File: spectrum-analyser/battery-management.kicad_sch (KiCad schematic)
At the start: 11 parts, among them J2 Conn_01x02, Q3 Q_NMOS_GSD, Q4 Q_NMOS_GSD, U5 AP9101CK6, U6 MCP73831-2-OT

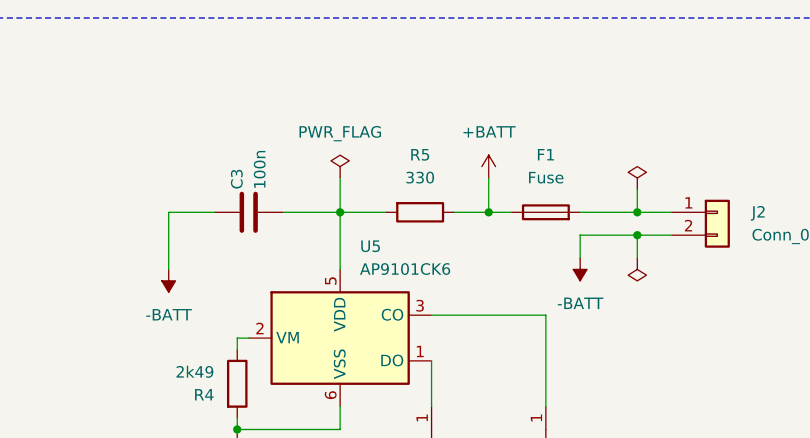
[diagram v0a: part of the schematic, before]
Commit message: Assign component footprints
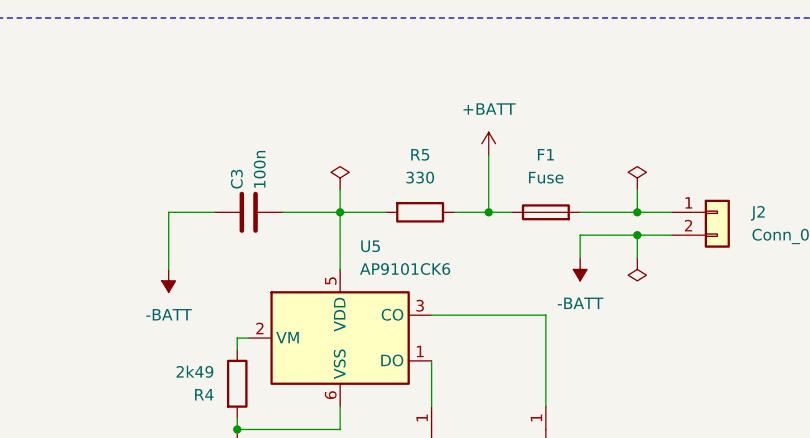
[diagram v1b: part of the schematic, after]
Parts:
- C3: footprint Capacitor_SMD:C_0603_1608Metric -> Capacitor_SMD:C_0603_1608Metric_Pad1.08x0.95mm_HandSolder
- F1: footprint (none) -> Fuse:Fuse_0603_1608Metric_Pad1.05x0.95mm_HandSolder
- J2: footprint (none) -> Connector_PinHeader_2.54mm:PinHeader_1x02_P2.54mm_Vertical
- JP1: footprint (none) -> Jumper:SolderJumper-2_P1.3mm_Open_RoundedPad1.0x1.5mm
- R4, R5: footprint Resistor_SMD:R_0603_1608Metric -> Resistor_SMD:R_0603_1608Metric_Pad0.98x0.95mm_HandSolder
- R6: footprint (none) -> Resistor_SMD:R_0603_1608Metric_Pad0.98x0.95mm_HandSolder
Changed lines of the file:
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@@
+	(wire
+		(pts
+			(xy 118.11 69.85) (xy 118.11 76.2)
+		)
+		(stroke
+			(width 0)
+			(type default)
+		)
+	)
 	(wire
 		(pts
@@
 	(wire
 		(pts
-			(xy 101.6 72.39) (xy 101.6 76.2)
-		)
-		(stroke
-			(width 0)
-			(type default)
-		)
-	)
-	(wire
-		(pts
 			(xy 138.43 78.74) (xy 134.62 78.74)
 		)
@@
 	(wire
 		(pts
-			(xy 118.11 76.2) (xy 118.11 72.39)
-		)
-		(stroke
-			(width 0)
-			(type default)
-		)
-	)
-	(wire
-		(pts
 			(xy 135.89 105.41) (xy 135.89 115.57)
 		)
@@
 		(pts
 			(xy 218.44 86.36) (xy 218.44 82.55)
+		)
+		(stroke
+			(width 0)
+			(type default)
+		)
+	)
+	(wire
+		(pts
+			(xy 101.6 73.66) (xy 101.6 76.2)
 		)
 		(stroke
@@
 			)
 		)
-		(property "Footprint" ""
+		(property "Footprint" "Jumper:SolderJumper-2_P1.3mm_Open_RoundedPad1.0x1.5mm"
 			(at 118.11 115.57 0)
 			(effects
@@
 			)
 		)
-		(property "Footprint" ""
+		(property "Footprint" "Connector_PinHeader_2.54mm:PinHeader_1x02_P2.54mm_Vertical"
 			(at 143.51 76.2 0)
 			(effects
@@
 	(symbol
 		(lib_id "power:PWR_FLAG")
-		(at 101.6 72.39 0)
+		(at 101.6 73.66 0)
 		(unit 1)
 		(exclude_from_sim no)
@@
 		(fields_autoplaced yes)
 		(property "Reference" "#FLG04"
-			(at 101.6 70.485 0)
+			(at 101.6 71.755 0)
 			(effects
 				(font
@@
 		)
 		(property "Value" "PWR_FLAG"
-			(at 101.6 67.31 0)
-			(effects
-				(font
-					(size 1.27 1.27)
-				)
+			(at 105.41 72.39 90)
+			(effects
+				(font
+					(size 1.27 1.27)
+				)
+				(hide yes)
 			)
 		)
 		(property "Footprint" ""
-			(at 101.6 72.39 0)
+			(at 101.6 73.66 0)
 			(effects
 				(font
@@
 		)
 		(property "Datasheet" "~"
-			(at 101.6 72.39 0)
+			(at 101.6 73.66 0)
 			(effects
 				(font
@@
 		)
 		(property "Description" "Special symbol for telling ERC where power comes from"
-			(at 101.6 72.39 0)
+			(at 101.6 73.66 0)
 			(effects
 				(font
@@
 			)
 		)
-		(property "Footprint" ""
+		(property "Footprint" "Resistor_SMD:R_0603_1608Metric_Pad0.98x0.95mm_HandSolder"
 			(at 196.85 98.298 90)
 			(effects
@@
 			)
 		)
-		(property "Footprint" ""
+		(property "Footprint" "Fuse:Fuse_0603_1608Metric_Pad1.05x0.95mm_HandSolder"
 			(at 124.46 77.978 90)
 			(effects
@@
 			)
 		)
-		(property "Footprint" "Resistor_SMD:R_0603_1608Metric"
+		(property "Footprint" "Resistor_SMD:R_0603_1608Metric_Pad0.98x0.95mm_HandSolder"
 			(at 110.49 74.422 90)
 			(effects
@@
 			)
 		)
-		(property "Footprint" "Capacitor_SMD:C_0603_1608Metric"
+		(property "Footprint" "Capacitor_SMD:C_0603_1608Metric_Pad1.08x0.95mm_HandSolder"
 			(at 95.25 75.2348 0)
 			(effects
@@
 			)
 		)
-		(property "Footprint" "Resistor_SMD:R_0603_1608Metric"
+		(property "Footprint" "Resistor_SMD:R_0603_1608Metric_Pad0.98x0.95mm_HandSolder"
 			(at 88.392 95.25 90)
 			(effects
@@
 	(symbol
 		(lib_id "power:+BATT")
-		(at 118.11 72.39 0)
+		(at 118.11 69.85 0)
 		(unit 1)
 		(exclude_from_sim no)
@@
 		(fields_autoplaced yes)
 		(property "Reference" "#PWR023"
-			(at 118.11 76.2 0)
+			(at 118.11 73.66 0)
 			(effects
 				(font
@@
 		)
 		(property "Value" "+BATT"
-			(at 118.11 67.31 0)
+			(at 118.11 64.77 0)
 			(effects
 				(font
@@
 		)
 		(property "Footprint" ""
-			(at 118.11 72.39 0)
+			(at 118.11 69.85 0)
 			(effects
 				(font
@@
 		)
 		(property "Datasheet" ""
-			(at 118.11 72.39 0)
+			(at 118.11 69.85 0)
 			(effects
 				(font
@@
 		)
 		(property "Description" "Power symbol creates a global label with name \"+BATT\""
-			(at 118.11 72.39 0)
-			(effects
-				(font
+			(at 118.11 69.85 0)
+			(effects
+				(font

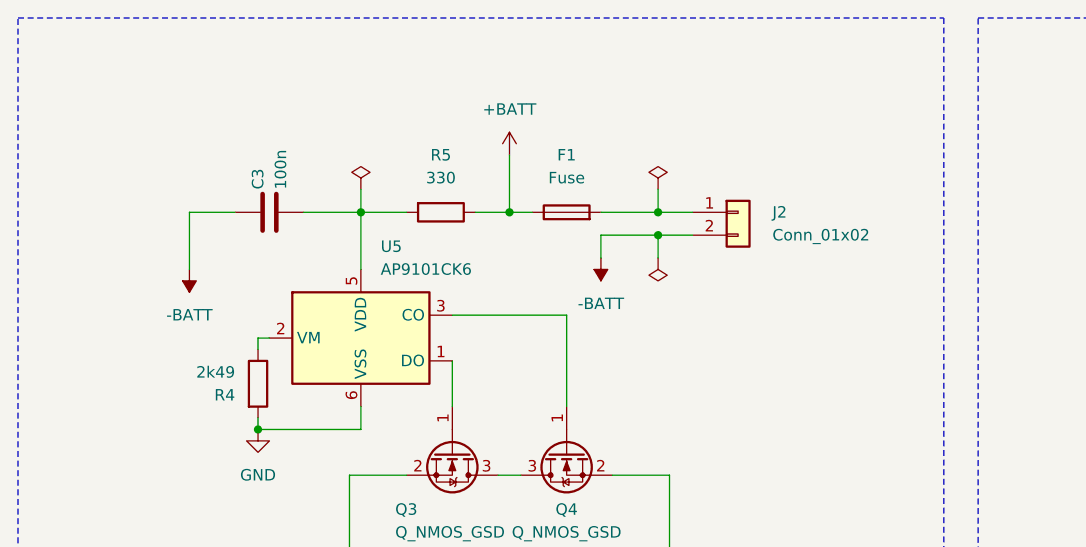
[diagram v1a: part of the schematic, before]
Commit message: Start initial PCB layout
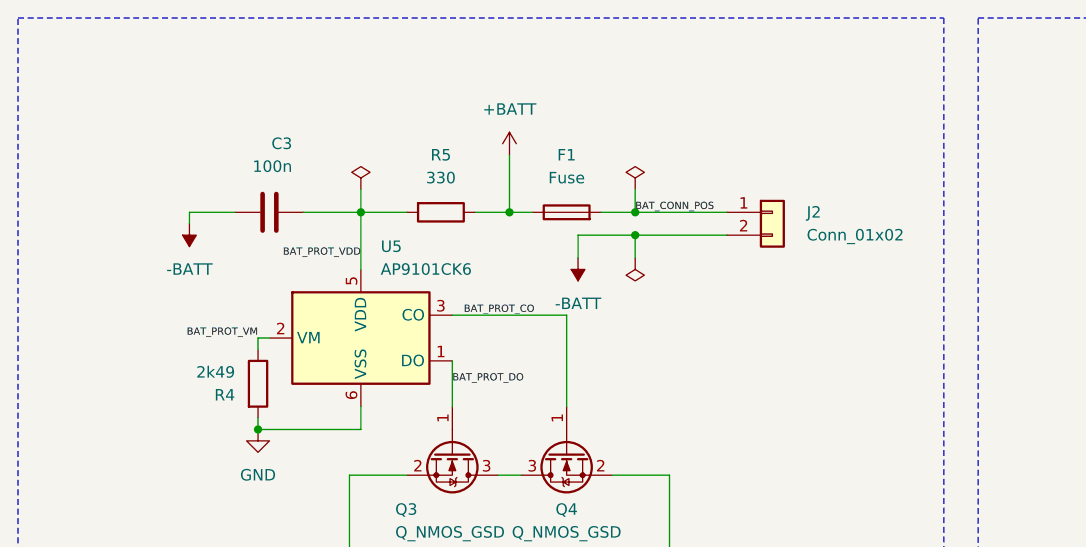
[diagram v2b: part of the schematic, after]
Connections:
- net BAT_CONN_POS: now reaches F1.2, J2.1 (Pin_1)
- net BAT_PROT_DO: now reaches Q3.1 (G), U5.1 (DO)
- net BAT_PROT_VDD: now reaches C3.2, R5.2, U5.5 (VDD)
- net BAT_PROT_VM: now reaches R4.1, U5.2 (VM)
- net BAT_PROT_CO: now reaches Q4.1 (G), U5.3 (CO)
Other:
- moved on the sheet: J2
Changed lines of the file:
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@@
 	)
 	(junction
-		(at 134.62 78.74)
+		(at 132.08 76.2)
 		(diameter 0)
 		(color 0 0 0 0)
@@
 	)
 	(junction
-		(at 134.62 76.2)
+		(at 132.08 78.74)
 		(diameter 0)
 		(color 0 0 0 0)
@@
 	(wire
 		(pts
-			(xy 134.62 76.2) (xy 138.43 76.2)
-		)
-		(stroke
-			(width 0)
-			(type default)
-		)
-	)
-	(wire
-		(pts
 			(xy 124.46 87.63) (xy 124.46 97.79)
 		)
@@
 	(wire
 		(pts
+			(xy 132.08 78.74) (xy 125.73 78.74)
+		)
+		(stroke
+			(width 0)
+			(type default)
+		)
+	)
+	(wire
+		(pts
 			(xy 218.44 91.44) (xy 215.9 91.44)
 		)
@@
 	(wire
 		(pts
-			(xy 134.62 78.74) (xy 134.62 81.28)
+			(xy 132.08 78.74) (xy 132.08 81.28)
 		)
 		(stroke
@@
 	(wire
 		(pts
-			(xy 128.27 76.2) (xy 134.62 76.2)
+			(xy 128.27 76.2) (xy 132.08 76.2)
 		)
 		(stroke
@@
 	(wire
 		(pts
-			(xy 82.55 82.55) (xy 82.55 76.2)
+			(xy 82.55 77.47) (xy 82.55 76.2)
 		)
 		(stroke
@@
 	(wire
 		(pts
-			(xy 128.27 78.74) (xy 128.27 81.28)
-		)
-		(stroke
-			(width 0)
-			(type default)
-		)
-	)
-	(wire
-		(pts
-			(xy 138.43 78.74) (xy 134.62 78.74)
+			(xy 125.73 78.74) (xy 125.73 81.28)
+		)
+		(stroke
+			(width 0)
+			(type default)
+		)
+	)
+	(wire
+		(pts
+			(xy 132.08 78.74) (xy 142.24 78.74)
 		)
 		(stroke
@@
 	(wire
 		(pts
-			(xy 134.62 78.74) (xy 128.27 78.74)
+			(xy 132.08 76.2) (xy 142.24 76.2)
 		)
 		(stroke
@@
 	(wire
 		(pts
-			(xy 134.62 73.66) (xy 134.62 76.2)
+			(xy 132.08 73.66) (xy 132.08 76.2)
 		)
 		(stroke
@@
 		)
 	)
+	(label "BAT_PROT_VDD"
+		(at 101.6 81.28 180)
+		(fields_autoplaced yes)
+		(effects
+			(font
+				(size 0.8 0.8)
+			)
+			(justify right bottom)
+		)
+	)
+	(label "BAT_CONN_POS"
+		(at 132.08 76.2 0)
+		(fields_autoplaced yes)
+		(effects
+			(font
+				(size 0.8 0.8)
+			)
+			(justify left bottom)
+		)
+	)
+	(label "BAT_PROT_VM"
+		(at 90.17 90.17 180)
+		(fields_autoplaced yes)
+		(effects
+			(font
+				(size 0.8 0.8)
+			)
+			(justify right bottom)
+		)
+	)
+	(label "BAT_PROT_DO"
+		(at 111.76 95.25 0)
+		(fields_autoplaced yes)
+		(effects
+			(font
+				(size 0.8 0.8)
+			)
+			(justify left bottom)
+		)
+	)
+	(label "BAT_PROT_CO"
+		(at 113.03 87.63 0)
+		(fields_autoplaced yes)
+		(effects
+			(font
+				(size 0.8 0.8)
+			)
+			(justify left bottom)
+		)
+	)
 	(global_label "CHRG_STAT"
 		(shape input)
@@
 	(symbol
 		(lib_id "power:PWR_FLAG")
-		(at 134.62 73.66 0)
+		(at 132.08 73.66 0)
 		(unit 1)
 		(exclude_from_sim no)
@@
 		(fields_autoplaced yes)
 		(property "Reference" "#FLG02"
-			(at 134.62 71.755 0)
+			(at 132.08 71.755 0)
 			(effects
 				(font
@@
 		)
 		(property "Value" "PWR_FLAG"
-			(at 134.62 68.58 0)
+			(at 132.08 68.58 0)
 			(effects
 				(font
@@
 		)
 		(property "Footprint" ""
-			(at 134.62 73.66 0)
+			(at 132.08 73.66 0)
 			(effects
 				(font
@@
 		)
 		(property "Datasheet" "~"
-			(at 134.62 73.66 0)
+			(at 132.08 73.66 0)
 			(effects
 				(font
@@
 		)
 		(property "Description" "Special symbol for telling ERC where power comes from"
-			(at 134.62 73.66 0)
+			(at 132.08 73.66 0)
 			(effects
 				(font
@@
 	(symbol
 		(lib_id "Connector_Generic:Conn_01x02")
-		(at 143.51 76.2 0)
+		(at 147.32 76.2 0)
 		(unit 1)
 		(exclude_from_sim no)
@@
 		(fields_autoplaced yes)
 		(property "Reference" "J2"
-			(at 147.32 76.1999 0)
+			(at 151.13 76.1999 0)
 			(effects
 				(font
@@
 		)
 		(property "Value" "Conn_01x02"
-			(at 147.32 78.7399 0)
+			(at 151.13 78.7399 0)
 			(effects
 				(font
@@
 		)
 		(property "Footprint" "Connector_PinHeader_2.54mm:PinHeader_1x02_P2.54mm_Vertical"
-			(at 143.51 76.2 0)
+			(at 147.32 76.2 0)
 			(effects
 				(font
@@
 		)
 		(property "Datasheet" "~"
-			(at 143.51 76.2 0)
+			(at 147.32 76.2 0)
 			(effects
 				(font
@@
 		)
 		(property "Description" "Generic connector, single row, 01x02, script generated (kicad-library-utils/schlib/autogen/connector/)"
-			(at 143.51 76.2 0)
+			(at 147.32 76.2 0)
 			(effects
 				(font
@@
 	(symbol
 		(lib_id "power:-BATT")
-		(at 82.55 82.55 180)
+		(at 82.55 77.47 180)
 		(unit 1)
 		(exclude_from_sim no)
@@
 		(fields_autoplaced yes)
 		(property "Reference" "#PWR020"
-			(at 82.55 78.74 0)
+			(at 82.55 73.66 0)
 			(effects
 				(font
@@
 		)
 		(property "Value" "-BATT"
-			(at 82.55 87.63 0)
+			(at 82.55 82.55 0)
 			(effects
 				(font
@@
 		)
 		(property "Footprint" ""
-			(at 82.55 82.55 0)
+			(at 82.55 77.47 0)
 			(effects
 				(font
@@
 		)
 		(property "Datasheet" ""
-			(at 82.55 82.55 0)
+			(at 82.55 77.47 0)
 			(effects
 				(font
@@
 		)
 		(property "Description" "Power symbol creates a global label with name \"-BATT\""
-			(at 82.55 82.55 0)
+			(at 82.55 77.47 0)
 			(effects
 				(font
@@
 	(symbol
 		(lib_id "power:PWR_FLAG")
-		(at 134.62 81.28 180)
+		(at 132.08 81.28 180)
 		(unit 1)
 		(exclude_from_sim no)
@@
 		(fields_autoplaced yes)
 		(property "Reference" "#FLG03"
-			(at 134.62 83.185 0)
+			(at 132.08 83.185 0)
 			(effects
 				(font
@@
 		)
 		(property "Value" "PWR_FLAG"
-			(at 134.62 86.36 0)
+			(at 132.08 86.36 0)
 			(effects
 				(font
@@
 		)
 		(property "Footprint" ""
-			(at 134.62 81.28 0)
+			(at 132.08 81.28 0)
 			(effects
 				(font
@@
 		)
 		(property "Datasheet" "~"
-			(at 134.62 81.28 0)
+			(at 132.08 81.28 0)
 			(effects
 				(font
@@
 		)
 		(property "Description" "Special symbol for telling ERC where power comes from"
-			(at 134.62 81.28 0)
+			(at 132.08 81.28 0)
 			(effects
 				(font
@@
 	(symbol
 		(lib_id "power:-BATT")
-		(at 128.27 81.28 180)
+		(at 125.73 81.28 180)
 		(unit 1)
 		(exclude_from_sim no)
@@
 		(fields_autoplaced yes)
 		(property "Reference" "#PWR024"
-			(at 128.27 77.47 0)
+			(at 125.73 77.47 0)
 			(effects
 				(font
@@
 		)
 		(property "Value" "-BATT"
-			(at 128.27 86.36 0)
+			(at 125.73 86.36 0)
 			(effects
 				(font
@@
 		)
 		(property "Footprint" ""
-			(at 128.27 81.28 0)
+			(at 125.73 81.28 0)
 			(effects
 				(font
@@
 		)
 		(property "Datasheet" ""
-			(at 128.27 81.28 0)
+			(at 125.73 81.28 0)
 			(effects
 				(font
@@
 		)
 		(property "Description" "Power symbol creates a global label with name \"-BATT\""
-			(at 128.27 81.28 0)
+			(at 125.73 81.28 0)
 			(effects
 				(font
@@
 		(dnp no)
 		(property "Reference" "C3"
-			(at 90.17 73.66 0)
+			(at 93.98 68.58 90)
 			(effects
 				(font
@@
 		)
 		(property "Value" "100n"
-			(at 92.71 73.66 0)
-			(effects
-				(font
+			(at 93.98 71.12 90)
+			(effects
+				(font

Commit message: Improve PCB layout
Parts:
- removed JP1: SolderJumper_2_Open, Jumper:SolderJumper-2_P1.3mm_Open_RoundedPad1.0x1.5mm, symbol Jumper:SolderJumper_2_Open
- added JP1: BAT_PROT_BYPASS, Jumper:SolderJumper-3_P1.3mm_Open_RoundedPad1.0x1.5mm, symbol Jumper:SolderJumper_3_Bridged12
- renumbered Q3 to Q4, Q4 to Q5, R4 to R6, R5 to R7, R6 to R8
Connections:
- net -BATT: now also JP1.2 (C); no longer C3.1, Q4.2 (S)
- net GND: now also JP1.3 (B)
- new net -BAT_PROT: C3.1, JP1.1 (A), Q4.2 (S)
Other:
- note added: "There is a solder jumper included here to bypass the battery protection IC if it required"
- note removed: "There is a solder bridge included here to bypass the battery protection IC if it is not installed"
- moved on the sheet: R6

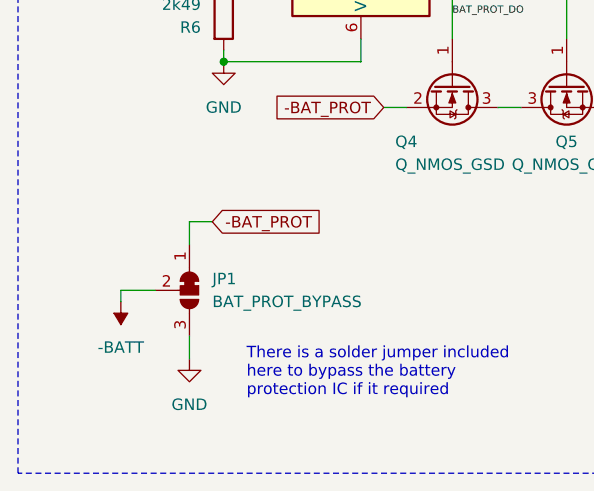
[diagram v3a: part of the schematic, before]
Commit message: Add informational silkscreen and change 3v3 LDO package
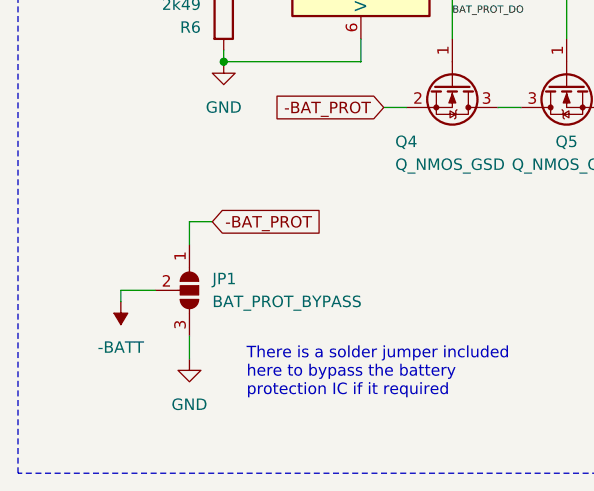
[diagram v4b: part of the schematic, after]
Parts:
- JP1: symbol Jumper:SolderJumper_3_Bridged12 -> Jumper:SolderJumper_3_Open
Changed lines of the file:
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@@
 	)
 	(symbol
-		(lib_id "Jumper:SolderJumper_3_Bridged12")
+		(lib_id "Jumper:SolderJumper_3_Open")
 		(at 82.55 125.73 270)
 		(unit 1)
@@
 			)
 		)
-		(property "Description" "3-pole Solder Jumper, pins 1+2 closed/bridged"
+		(property "Description" "Solder Jumper, 3-pole, open"
 			(at 82.55 125.73 0)
 			(effects

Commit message: Assign component values and add charger capacitors
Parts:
- added C4, C5: 4u7, Capacitor_SMD:C_0603_1608Metric_Pad1.08x0.95mm_HandSolder, symbol Device:C
- F1: value Fuse -> 3A
- R8: value 12k -> 10k
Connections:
- net +BATT: now also C5.1
- net GND: now also C4.2, C5.2
- net VUSB: now also C4.1

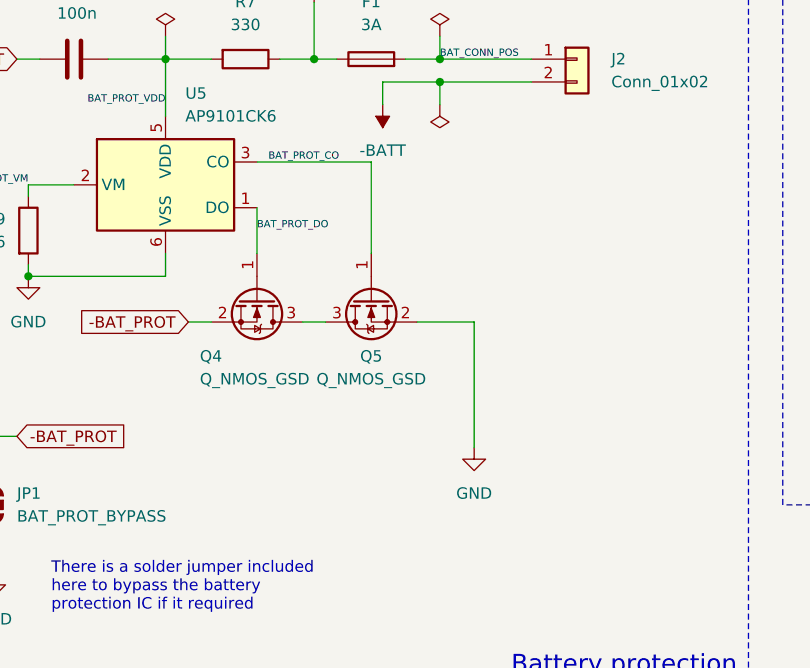
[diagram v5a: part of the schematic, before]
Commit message: Re-organise battery management sections
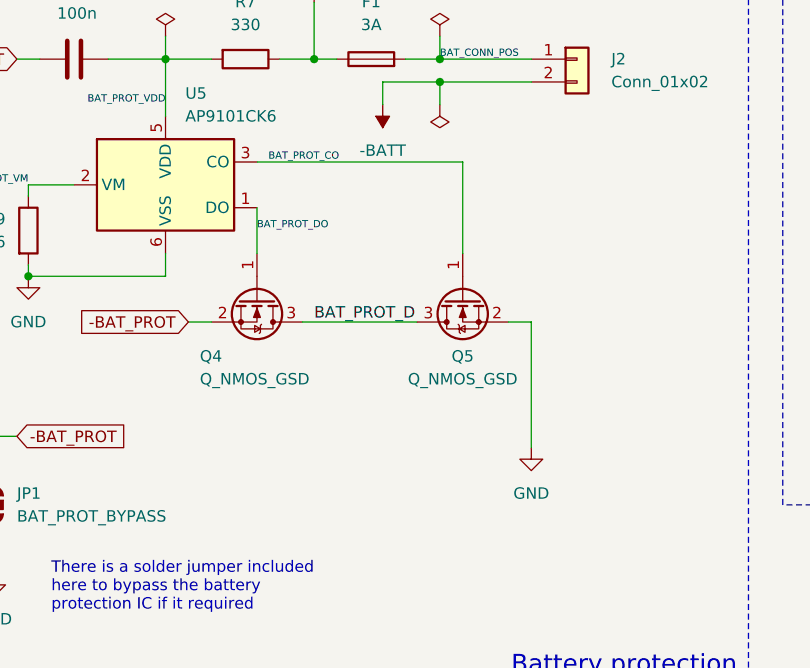
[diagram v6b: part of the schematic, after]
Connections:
- net BAT_PROT_D: now reaches Q4.3 (D), Q5.3 (D)
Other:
- moved on the sheet: Q5
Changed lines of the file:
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@@
 	(wire
 		(pts
-			(xy 124.46 87.63) (xy 124.46 97.79)
+			(xy 134.62 87.63) (xy 134.62 97.79)
 		)
 		(stroke
@@
 	(wire
 		(pts
+			(xy 116.84 105.41) (xy 129.54 105.41)
+		)
+		(stroke
+			(width 0)
+			(type default)
+		)
+	)
+	(wire
+		(pts
 			(xy 240.03 76.2) (xy 240.03 78.74)
 		)
@@
 	(wire
 		(pts
-			(xy 111.76 87.63) (xy 124.46 87.63)
+			(xy 111.76 87.63) (xy 134.62 87.63)
 		)
 		(stroke
@@
 	(wire
 		(pts
-			(xy 129.54 105.41) (xy 135.89 105.41)
+			(xy 139.7 105.41) (xy 142.24 105.41)
 		)
 		(stroke
@@
 	(wire
 		(pts
-			(xy 135.89 105.41) (xy 135.89 119.38)
+			(xy 142.24 105.41) (xy 142.24 119.38)
 		)
 		(stroke
@@
 		(pts
 			(xy 215.9 86.36) (xy 218.44 86.36)
-		)
-		(stroke
-			(width 0)
-			(type default)
-		)
-	)
-	(wire
-		(pts
-			(xy 119.38 105.41) (xy 116.84 105.41)
 		)
 		(stroke
@@
 		)
 	)
+	(label "BAT_PROT_D"
+		(at 118.11 105.41 0)
+		(fields_autoplaced yes)
+		(effects
+			(font
+				(size 1.27 1.27)
+			)
+			(justify left bottom)
+		)
+	)
 	(label "BAT_PROT_VM"
 		(at 86.36 90.17 180)
@@
 	(symbol
 		(lib_id "power:GND")
-		(at 135.89 119.38 0)
+		(at 142.24 119.38 0)
 		(unit 1)
 		(exclude_from_sim no)
@@
 		(fields_autoplaced yes)
 		(property "Reference" "#PWR031"
-			(at 135.89 125.73 0)
+			(at 142.24 125.73 0)
 			(effects
 				(font
@@
 		)
 		(property "Value" "GND"
-			(at 135.89 124.46 0)
+			(at 142.24 124.46 0)
 			(effects
 				(font
@@
 		)
 		(property "Footprint" ""
-			(at 135.89 119.38 0)
+			(at 142.24 119.38 0)
 			(effects
 				(font
@@
 		)
 		(property "Datasheet" ""
-			(at 135.89 119.38 0)
+			(at 142.24 119.38 0)
 			(effects
 				(font
@@
 		)
 		(property "Description" "Power symbol creates a global label with name \"GND\" , ground"
-			(at 135.89 119.38 0)
+			(at 142.24 119.38 0)
 			(effects
 				(font
@@
 	(symbol
 		(lib_id "Device:Q_NMOS_GSD")
-		(at 124.46 102.87 90)
+		(at 134.62 102.87 90)
 		(mirror x)
 		(unit 1)
@@
 		(dnp no)
 		(property "Reference" "Q5"
-			(at 124.46 109.22 90)
+			(at 134.62 109.22 90)
 			(effects
 				(font
@@
 		)
 		(property "Value" "Q_NMOS_GSD"
-			(at 124.46 111.76 90)
+			(at 134.62 111.76 90)
 			(effects
 				(font
@@
 		)
 		(property "Footprint" "Package_TO_SOT_SMD:SOT-23"
-			(at 121.92 107.95 0)
+			(at 132.08 107.95 0)
 			(effects
 				(font
@@
 		)
 		(property "Datasheet" "~"
-			(at 124.46 102.87 0)
+			(at 134.62 102.87 0)
 			(effects
 				(font
@@
 		)
 		(property "Description" ""
-			(at 124.46 102.87 0)
-			(effects
-				(font
+			(at 134.62 102.87 0)
+			(effects
+				(font
